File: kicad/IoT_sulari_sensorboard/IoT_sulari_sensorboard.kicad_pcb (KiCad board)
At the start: 2 copper layers, 12.9 x 17.5 mm, 8 parts, among them J1 20021121-00010C4LF, U1 SHT40-AD1B-R3, U2 TMP117MAIDRVT

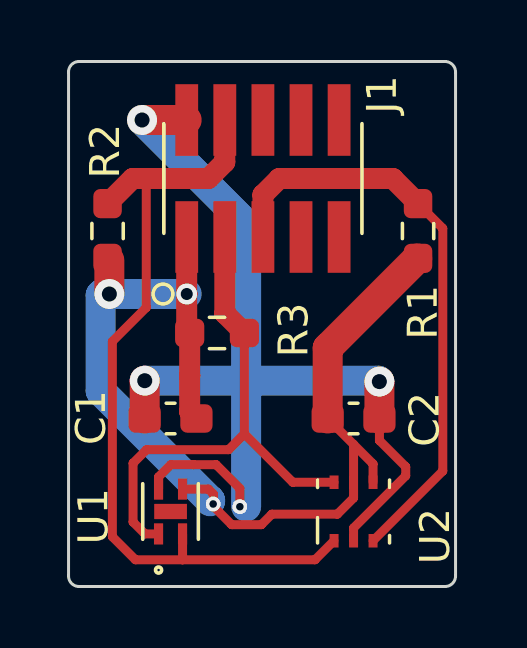
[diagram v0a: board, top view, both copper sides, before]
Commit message: sensorboard modify and mainboard connector add
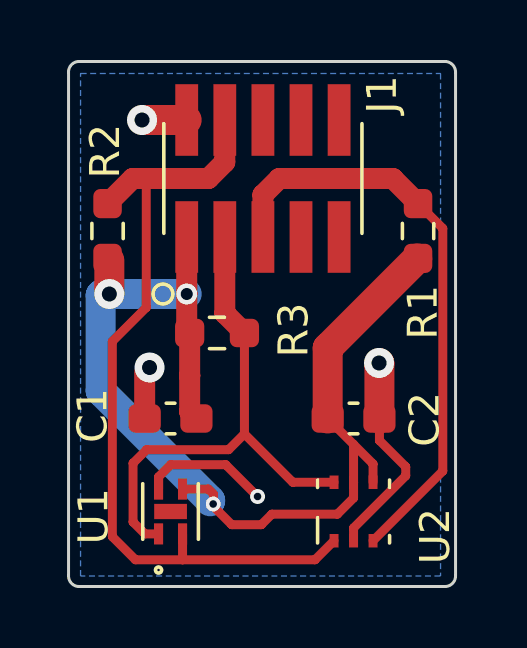
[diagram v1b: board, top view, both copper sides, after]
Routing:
- net /GND: track 35.5 -> 14.6 mm
- added copper zone on B.Cu, net /GND
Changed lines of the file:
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@@
     (property "ki_keywords" "cap capacitor")
     (attr smd)
-    (fp_text reference "C1" (at 2.65 0.03 90) (layer "F.SilkS")
+    (fp_text reference "C1" (at 2.6 0.1 90) (layer "F.SilkS")
         (effects (font (size 1 1) (thickness 0.15)))
     )
@@
   (segment (start 132.67 93.08) (end 136.32 96.73) (width 1) (layer "B.Cu") (net 1))
   (segment (start 136.32 96.73) (end 136.32 96.76) (width 1) (layer "B.Cu") (net 1))
-  (segment (start 137.31 96.87) (end 137.32 96.88) (width 0.3) (layer "F.Cu") (net 2))
+  (segment (start 134.600001 96.3531) (end 134.600001 95.947099) (width 0.3) (layer "F.Cu") (net 2))
   (segment (start 141.1 97.65) (end 142.84 95.91) (width 0.3) (layer "F.Cu") (net 2))
   (segment (start 142.84 95.91) (end 142.84 95.61) (width 0.3) (layer "F.Cu") (net 2))
-  (segment (start 134.600001 96.3531) (end 134.600001 95.947099) (width 0.3) (layer "F.Cu") (net 2))
-  (segment (start 141.9625 92.7725) (end 141.96 92.77) (width 1) (layer "F.Cu") (net 2))
+  (segment (start 134.600001 95.947099) (end 135.0071 95.54) (width 0.3) (layer "F.Cu") (net 2))
   (segment (start 141.1 98.074999) (end 141.1 97.65) (width 0.3) (layer "F.Cu") (net 2))
   (segment (start 135.5385 84.049999) (end 134.05 84.05) (width 1) (layer "F.Cu") (net 2))
-  (segment (start 137.31 96.33) (end 137.31 96.87) (width 0.3) (layer "F.Cu") (net 2))
+  (segment (start 141.95 92.15) (end 141.9625 92.1625) (width 1) (layer "F.Cu") (net 2))
+  (segment (start 134.1375 92.4625) (end 134.3 92.3) (width 0.25) (layer "F.Cu") (net 2))
   (segment (start 141.9625 94.7325) (end 141.9625 94) (width 0.3) (layer "F.Cu") (net 2))
+  (segment (start 134.1375 94) (end 134.1375 92.4625) (width 0.7) (layer "F.Cu") (net 2))
   (segment (start 142.84 95.61) (end 141.9625 94.7325) (width 0.3) (layer "F.Cu") (net 2))
-  (segment (start 135.76 95.54) (end 136.52 95.54) (width 0.3) (layer "F.Cu") (net 2))
-  (segment (start 136.52 95.54) (end 137.31 96.33) (width 0.3) (layer "F.Cu") (net 2))
-  (segment (start 134.1375 92.7425) (end 134.14 92.74) (width 1) (layer "F.Cu") (net 2))
-  (segment (start 135.0071 95.54) (end 135.76 95.54) (width 0.3) (layer "F.Cu") (net 2))
-  (segment (start 134.600001 95.947099) (end 135.0071 95.54) (width 0.3) (layer "F.Cu") (net 2))
-  (segment (start 141.9625 94) (end 141.9625 92.7725) (width 1) (layer "F.Cu") (net 2))
-  (segment (start 134.1375 94) (end 134.1375 92.7425) (width 1) (layer "F.Cu") (net 2))
-  (via (at 134.14 92.74) (size 1) (drill 0.5) (layers "F.Cu" "B.Cu") (net 2))
+  (segment (start 135.0071 95.54) (end 136.84 95.54) (width 0.3) (layer "F.Cu") (net 2))
+  (segment (start 136.84 95.54) (end 137.9 96.6) (width 0.3) (layer "F.Cu") (net 2))
+  (segment (start 141.9625 92.1625) (end 141.9625 94) (width 1) (layer "F.Cu") (net 2))
+  (via (at 134.3 92.3) (size 1) (drill 0.5) (layers "F.Cu" "B.Cu") (net 2))
   (via (at 134.05 84.05) (size 1) (drill 0.5) (layers "F.Cu" "B.Cu") (net 2))
-  (via (at 141.96 92.77) (size 1) (drill 0.5) (layers "F.Cu" "B.Cu") (net 2))
-  (via (at 137.31 96.94) (size 0.5) (drill 0.25) (layers "F.Cu" "B.Cu") (net 2))
-  (segment (start 134.05 84.05) (end 137.52 87.52) (width 1) (layer "B.Cu") (net 2))
-  (segment (start 141.93 92.74) (end 141.96 92.77) (width 1) (layer "B.Cu") (net 2))
-  (segment (start 137.52 87.52) (end 137.52 96.94) (width 1) (layer "B.Cu") (net 2))
-  (segment (start 134.14 92.74) (end 141.93 92.74) (width 1) (layer "B.Cu") (net 2))
+  (via (at 141.95 92.15) (size 1) (drill 0.5) (layers "F.Cu" "B.Cu") (net 2))
+  (via (at 137.9 96.6) (size 0.5) (drill 0.25) (layers "F.Cu" "B.Cu") (net 2))
   (segment (start 139.075001 96.125001) (end 140.449999 96.125001) (width 0.3) (layer "F.Cu") (net 3))
   (segment (start 133.75 97.449699) (end 133.75 95.49) (width 0.3) (layer "F.Cu") (net 3))
@@
   (segment (start 142.4125 86) (end 143.25 86.8375) (width 0.7) (layer "F.Cu") (net 5))
   (segment (start 138.0785 86.545201) (end 138.623701 86) (width 0.7) (layer "F.Cu") (net 5))
+  (zone (net 2) (net_name "/GND") (layer "B.Cu") (hatch edge 0.5)
+    (connect_pads (clearance 0.5))
+    (min_thickness 0.25) (filled_areas_thickness no)
+    (fill yes (thermal_gap 0.5) (thermal_bridge_width 0.5))
+    (polygon
+      (pts
+        (xy 132 82.5)
+        (xy 144 82.5)
+        (xy 144 99.25)
+        (xy 132 99.25)
+      )
+    )
+  )
 )
